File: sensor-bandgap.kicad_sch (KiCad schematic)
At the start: 0 parts

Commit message: ldo and buck updated, footprints added
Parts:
- added R34, R35: R, symbol Device:R
- added U12: ALD1107PBL, footprints9:14-PDIP_ALD, symbol pmosquad:ALD1107PBL
- added U15: 300P14-U, 300P14-U:DIP794W46P254L1917H432Q14, symbol 300P14-U:300P14-U
- added U16, U18: OPA705PA, footprints10:P8, symbol opa705:OPA705PA
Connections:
- new net: R34.1, U15.1, U15.2
- new net: U15.11, U15.4
- new net GND: U15.10, U15.12, U15.3, U15.5, U16.4 (V-), U18.4 (V-)
- new net PTAT_current: U12.14 (DP2)
- new net PWR_IN: U12.11 (V+), U12.12 (SP2), U12.3 (SP1), U12.7 (SP4), U12.8 (SP3), U16.7 (V+), U18.7 (V+)
- new net bandgap_volt: U18.2 (IN-), U18.6 (OUT)
- new net collect: R35.2, U15.13, U15.14, U15.8, U15.9
- new net feed: U12.13 (GP2), U12.2 (GP1), U12.6 (GP4), U12.9 (GP3), U16.6 (OUT)
- new net minus: U12.1 (DP1), U15.6, U15.7, U16.2 (IN-)
- new net plus: R35.1, U12.10 (DP3), U16.3 (IN+)
- new net vref: R34.2, U12.5 (DP4), U18.3 (IN+)

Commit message: schematic cleanup
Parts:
- R34, R35: footprint (none) -> Resistor_SMD:R_0805_2012Metric
- U12: footprint footprints9:14-PDIP_ALD -> footprints:14-PDIP_ALD
- U15: footprint 300P14-U:DIP794W46P254L1917H432Q14 -> footprints:300P14-U
- U16, U18: footprint footprints10:P8 -> footprints:P8
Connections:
- net PWR_IN: no longer U12.11 (V+)
- no-connect marks 0 -> 8
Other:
- moved on the sheet: R34, R35, U12, U15, U16

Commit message: pcb layout
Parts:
- added C25, C46, C47: C_Polarized, Capacitor_SMD:C_0805_2012Metric, symbol Device:C
- added Q8: NPN, Package_TO_SOT_THT:TO-220-3_Horizontal_TabDown, symbol Simulation_SPICE:NPN
- added R45: R, Resistor_SMD:R_0805_2012Metric, symbol Device:R
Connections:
- net GND: now also C25.2, C46.2, C47.2
- net PWR_IN: now also Q8.1 (C), R45.2; no longer U12.12 (SP2), U12.3 (SP1), U12.7 (SP4), U12.8 (SP3), U16.7 (V+), U18.7 (V+)
- new net: C25.1, Q8.2 (B), R45.1
- new net pwr_bus: C46.1, C47.1, Q8.3 (E), U12.12 (SP2), U12.3 (SP1), U12.7 (SP4), U12.8 (SP3), U16.7 (V+), U18.7 (V+)
- no-connect marks 8 -> 9

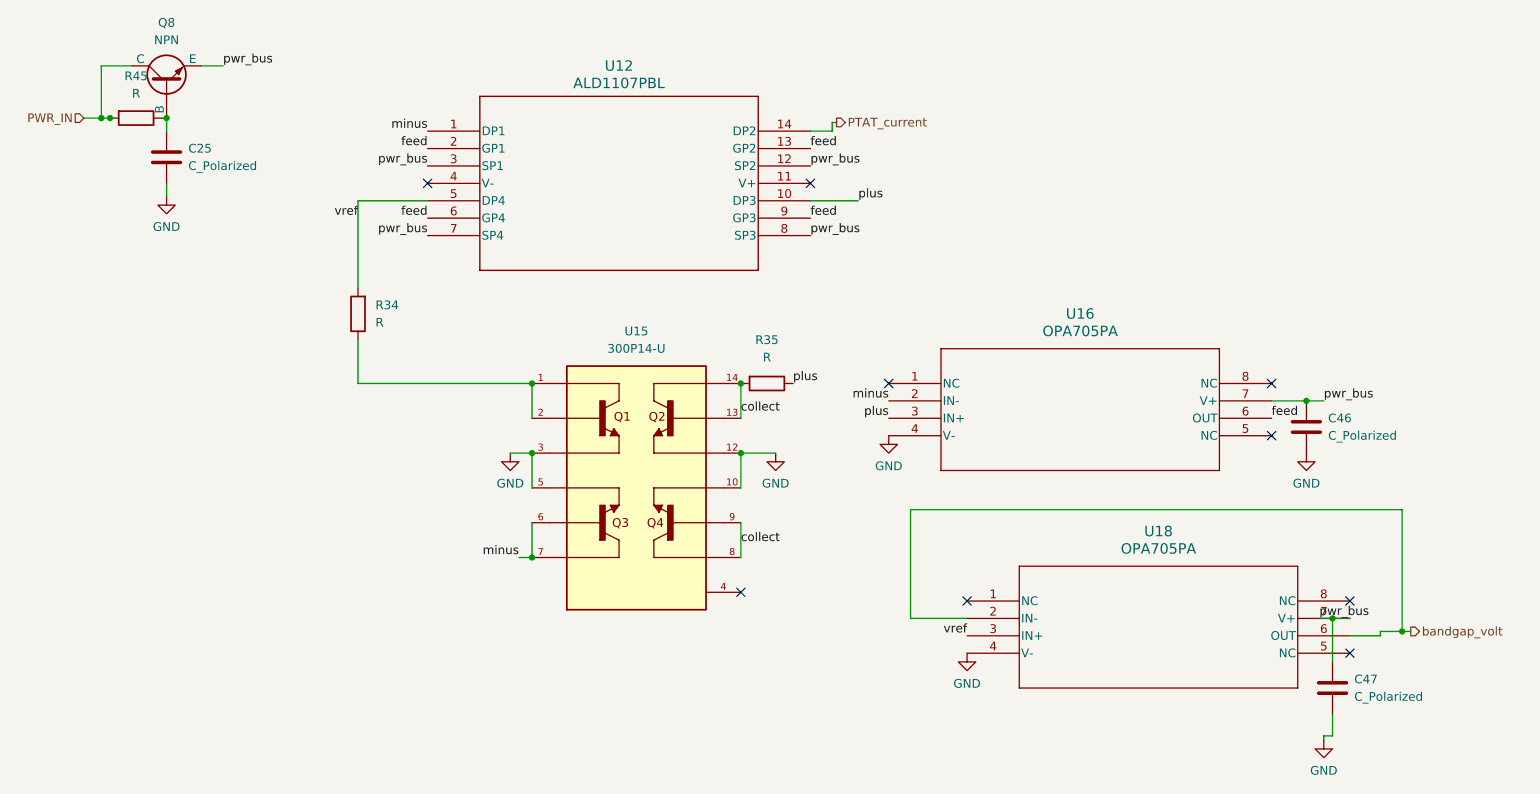
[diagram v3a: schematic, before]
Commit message: pcb layout component placement 90% done
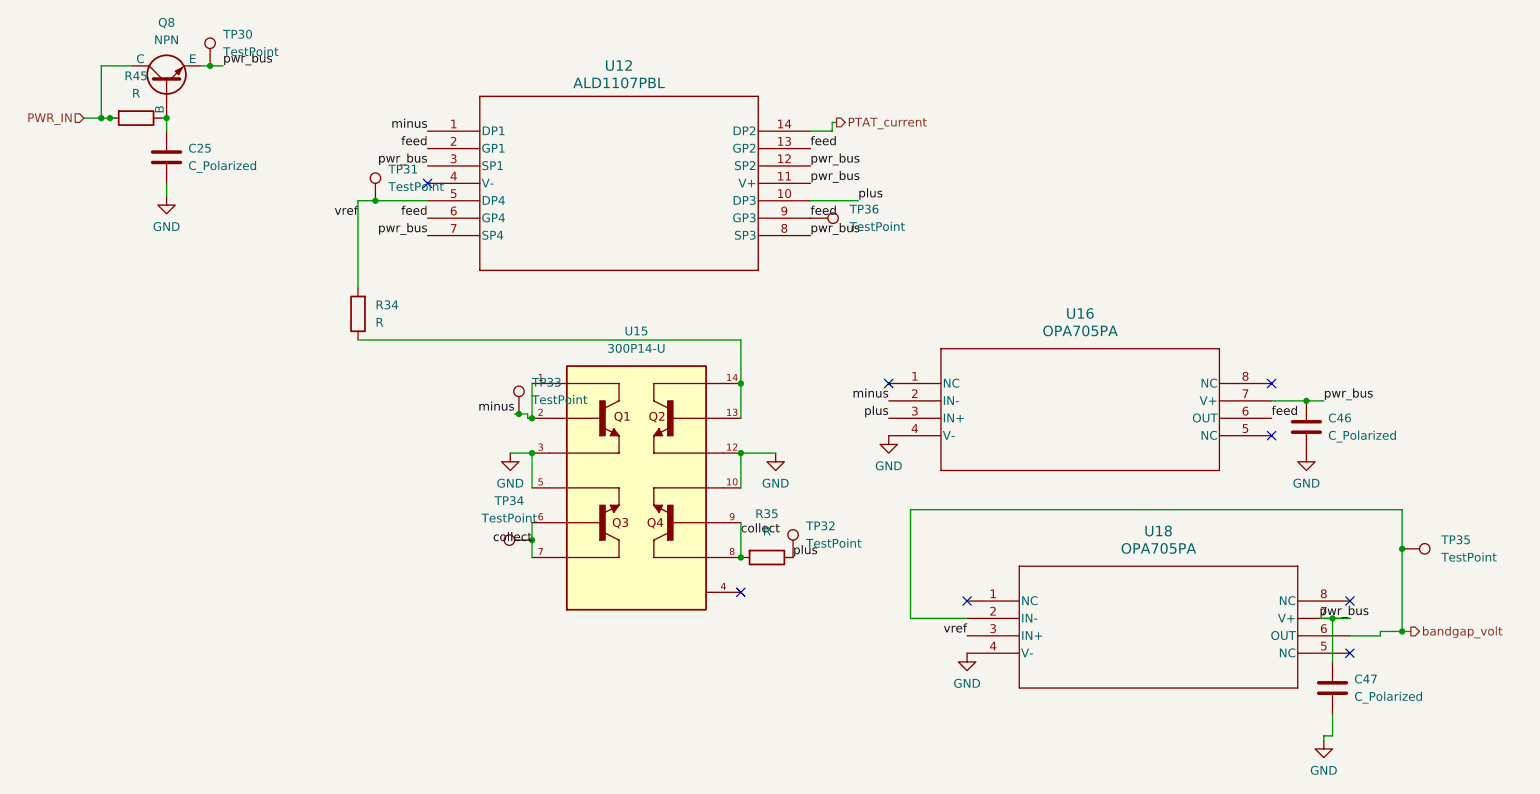
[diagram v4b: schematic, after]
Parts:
- added TP30, TP31, TP32, TP33, TP34, TP35, TP36: TestPoint, TestPoint:TestPoint_Plated_Hole_D2.0mm, symbol Connector:TestPoint
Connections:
- net bandgap_volt: now also TP35.1
- net collect: now also U15.6, U15.7, TP34.1; no longer U15.13, U15.14
- net feed: now also TP36.1
- net minus: now also U15.1, U15.2, TP33.1; no longer U15.6, U15.7
- net plus: now also TP32.1
- net pwr_bus: now also U12.11 (V+), TP30.1
- net vref: now also TP31.1
- new net: R34.1, U15.13, U15.14
- no-connect marks 9 -> 8
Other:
- moved on the sheet: R35

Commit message: pcb layout draft
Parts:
- C25, C46, C47: footprint Capacitor_SMD:C_0805_2012Metric -> footprints_pretty:0805_cap_nosilk
- R34, R35, R45: footprint Resistor_SMD:R_0805_2012Metric -> footprints_pretty:res_0805_nosilk
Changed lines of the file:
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@@
 			)
 		)
-		(property "Footprint" "Resistor_SMD:R_0805_2012Metric"
+		(property "Footprint" "footprints_pretty:res_0805_nosilk"
 			(at 43.815 59.817 90)
 			(effects
@@
 			)
 		)
-		(property "Footprint" "Capacitor_SMD:C_0805_2012Metric"
+		(property "Footprint" "footprints_pretty:0805_cap_nosilk"
 			(at 219.4052 148.59 0)
 			(effects
@@
 			)
 		)
-		(property "Footprint" "Resistor_SMD:R_0805_2012Metric"
+		(property "Footprint" "footprints_pretty:res_0805_nosilk"
 			(at 135.89 123.952 90)
 			(effects
@@
 			)
 		)
-		(property "Footprint" "Capacitor_SMD:C_0805_2012Metric"
+		(property "Footprint" "footprints_pretty:0805_cap_nosilk"
 			(at 215.5952 110.49 0)
 			(effects
@@
 			)
 		)
-		(property "Footprint" "Capacitor_SMD:C_0805_2012Metric"
+		(property "Footprint" "footprints_pretty:0805_cap_nosilk"
 			(at 49.2252 71.12 0)
 			(effects
@@
 			)
 		)
-		(property "Footprint" "Resistor_SMD:R_0805_2012Metric"
+		(property "Footprint" "footprints_pretty:res_0805_nosilk"
 			(at 77.978 90.17 90)
 			(effects

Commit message: changed values
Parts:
- C25: value C_Polarized -> 10uF
- Q8: value NPN -> NPN 40V
- R34: value R -> 1.87k
- R35: value R -> 63
- R45: value R -> 400
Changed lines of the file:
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@@
 			)
 		)
-		(property "Value" "R"
+		(property "Value" "400"
 			(at 43.815 58.0119 90)
 			(effects
@@
 			)
 		)
-		(property "Value" "R"
+		(property "Value" "63"
 			(at 135.89 121.92 90)
 			(effects
@@
 			)
 		)
-		(property "Value" "C_Polarized"
+		(property "Value" "10uF"
 			(at 51.435 68.5799 0)
 			(effects
@@
 			)
 		)
-		(property "Value" "NPN"
+		(property "Value" "NPN 40V"
 			(at 48.26 50.2103 90)
 			(effects
@@
 			)
 		)
-		(property "Value" "R"
+		(property "Value" "1.87k"
 			(at 78.74 91.4399 0)
 			(effects
